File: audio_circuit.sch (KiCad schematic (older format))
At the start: 21 parts

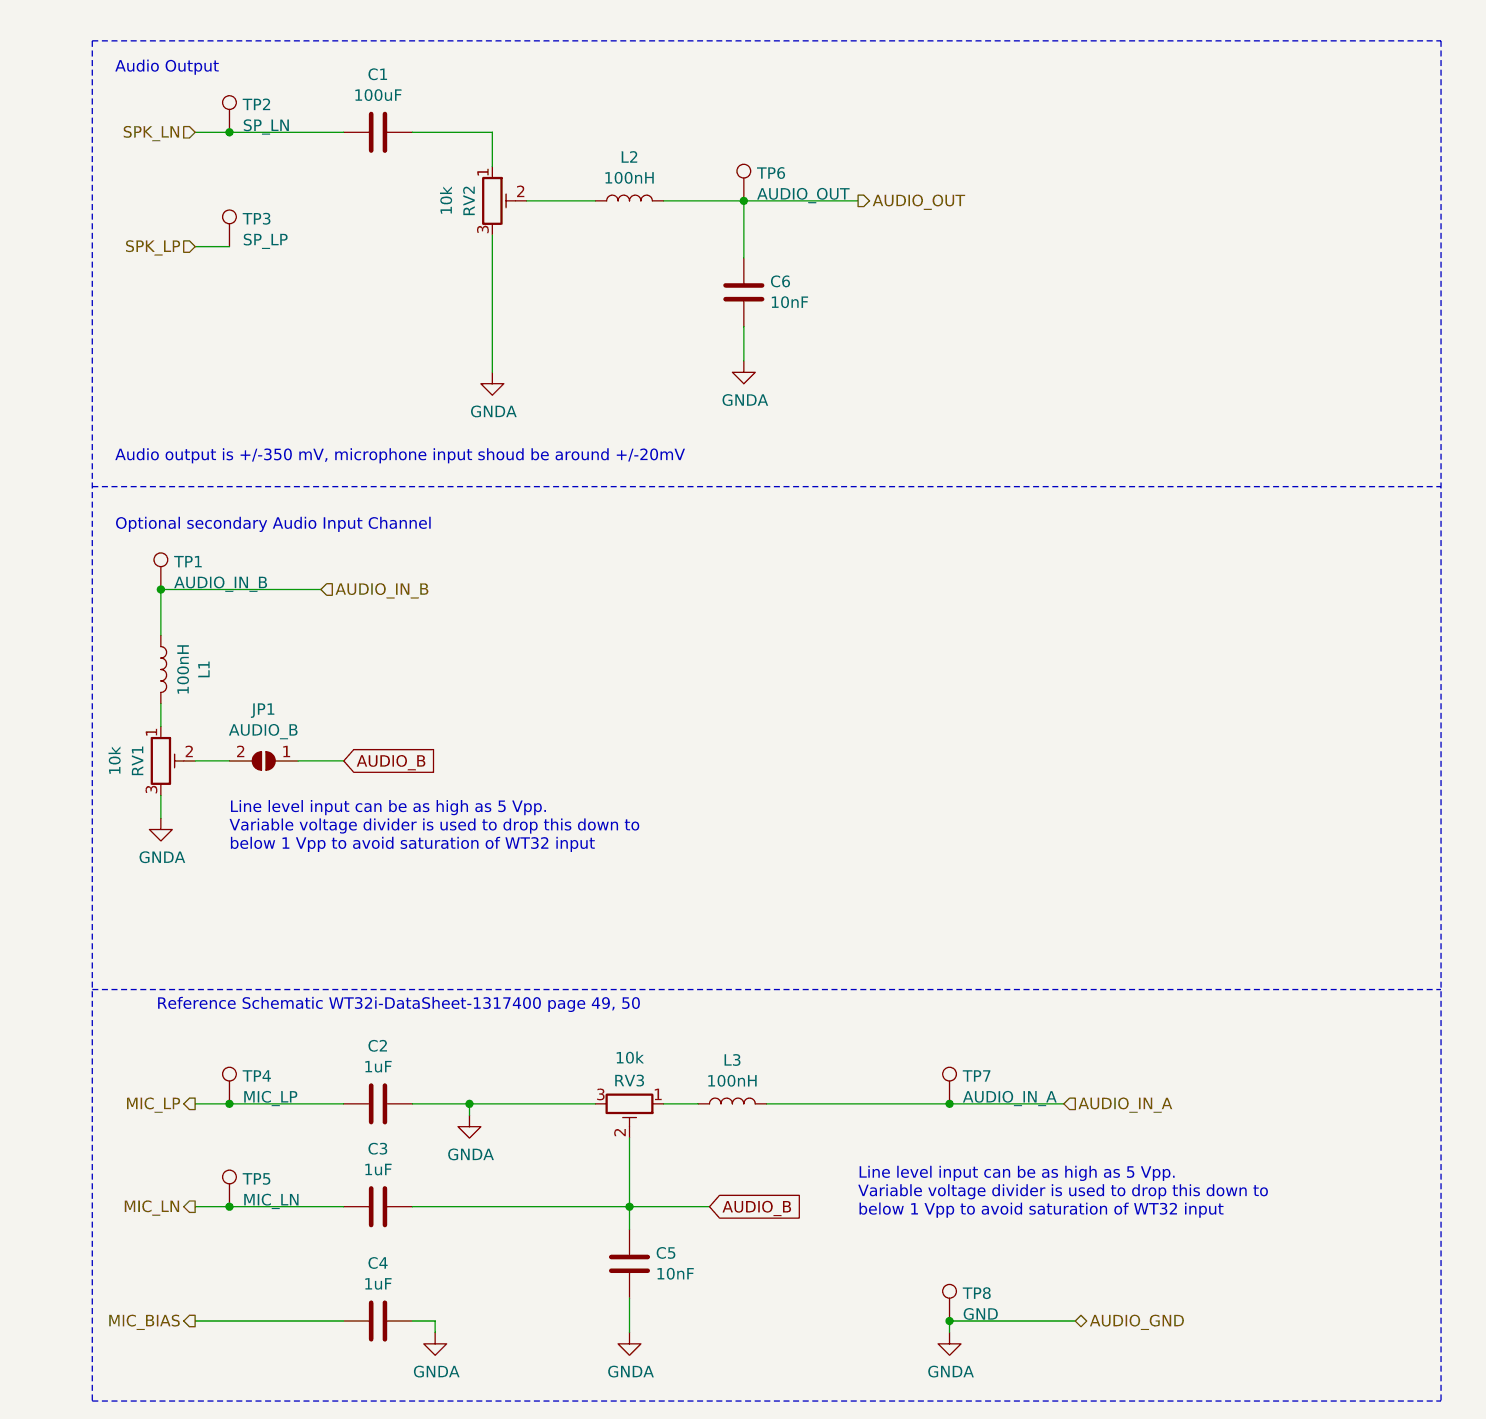
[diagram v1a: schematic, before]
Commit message: [#1] Refined Schematic
* Removed RTS CTS
* Added 15pF capacitator to audio IN+
* Removed PTT jumper
* Added pull-up jumper
* Added solder jmpr bypass to RV
* Changed button footprint to SMD version
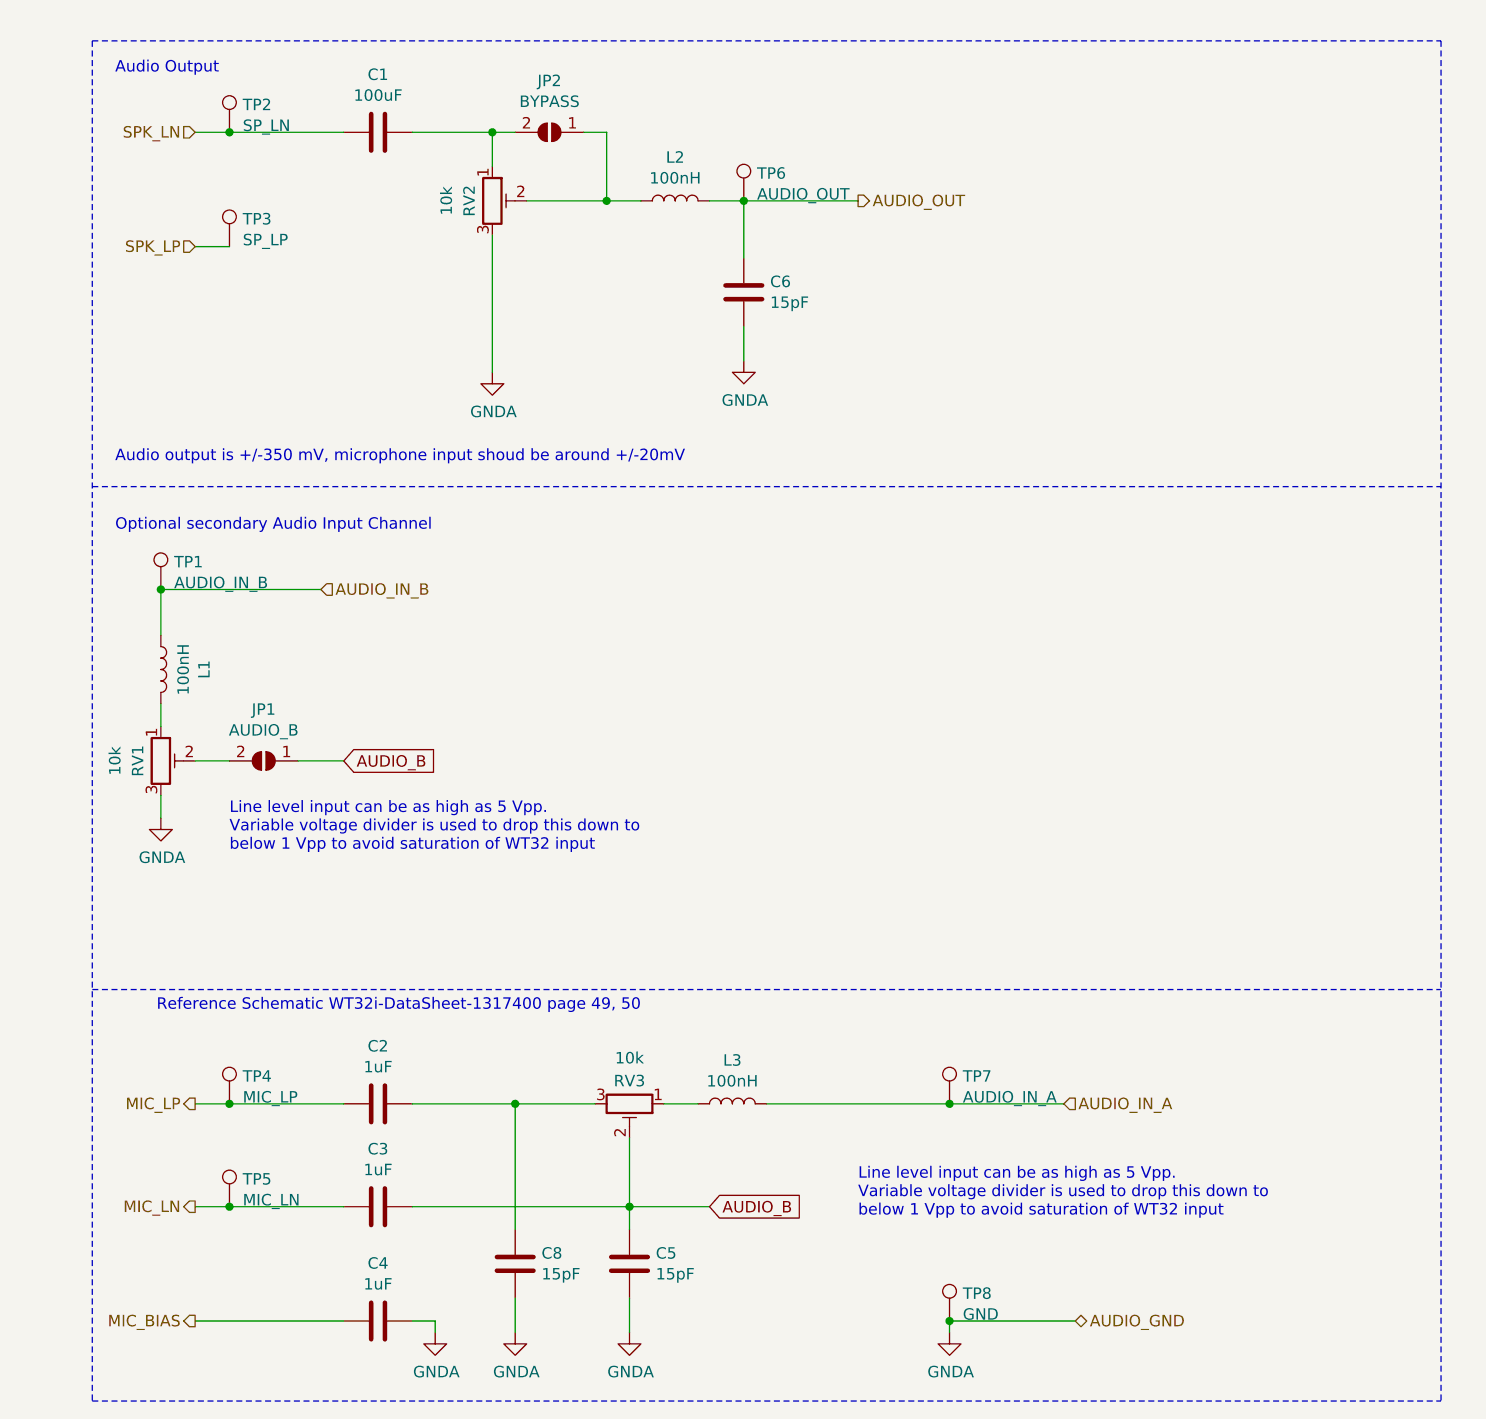
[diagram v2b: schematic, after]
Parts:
- added C8: 15pF, Capacitor_SMD:C_0805_2012Metric_Pad1.15x1.40mm_HandSolder, symbol Device:C
- added JP2: BYPASS, Jumper:SolderJumper-2_P1.3mm_Open_TrianglePad1.0x1.5mm, symbol Jumper:SolderJumper_2_Open
- C1: Mouser Best.Nr. 581-F980J107MSA -> TBD; Notes (none) -> Tantal neccessary?
- C2, C3, C4: Mouser Best.Nr. 581-F981V105MSA -> TBD; Notes (none) -> Tantal neccessary?
- C5, C6: value 10nF -> 15pF; Mouser Best.Nr. 710-885012207092 -> TBD; Notes (none) -> Tantal neccessary?
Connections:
- net GNDA: now also C8.2; no longer C2.1, RV3.3
- net at C1.1, RV2.1: now also JP2.2 (B)
- net at L2.1, RV2.2: now also JP2.1 (A)
- new net: C2.1, C8.1, RV3.3
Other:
- moved on the sheet: L2
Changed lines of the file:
@@
 EESchema Schematic File Version 4
 LIBS:bt-trx-dev-board-cache
-EELAYER 26 0
+EELAYER 29 0
 EELAYER END
 $Descr A4 11693 8268
@@
 F 2 "Capacitor_SMD:C_0805_2012Metric_Pad1.15x1.40mm_HandSolder" H 2088 6700 50  0001 C CNN
 F 3 "~" H 2050 6850 50  0001 C CNN
-F 4 "" H 300 0   50  0001 C CNN "Reichelt Best.Nr."
-F 5 "581-F981V105MSA" H 300 0   50  0001 C CNN "Mouser Best.Nr."
+F 4 "TBD" H 300 0   50  0001 C CNN "Mouser Best.Nr."
+F 5 "Tantal neccessary?" H 2050 6850 50  0001 C CNN "Notes"
 	1    2050 6850
 	0    1    1    0
@@
 F 2 "Inductor_SMD:L_0805_2012Metric_Pad1.15x1.40mm_HandSolder" H 3600 5900 50  0001 C CNN
 F 3 "~" H 3600 5900 50  0001 C CNN
-F 4 "" H 300 -100 50  0001 C CNN "Reichelt Best.Nr."
-F 5 "810-MLF2012DR10MT000" H 300 -100 50  0001 C CNN "Mouser Best.Nr."
+F 4 "810-MLF2012DR10MT000" H 300 -100 50  0001 C CNN "Mouser Best.Nr."
 	1    3600 5900
 	0    -1   -1   0
@@
 P 3150 6600
 F 0 "C5" H 3265 6646 50  0000 L CNN
-F 1 "10nF" H 3265 6555 50  0000 L CNN
+F 1 "15pF" H 3265 6555 50  0000 L CNN
 F 2 "Capacitor_SMD:C_0805_2012Metric_Pad1.15x1.40mm_HandSolder" H 3188 6450 50  0001 C CNN
 F 3 "~" H 3150 6600 50  0001 C CNN
-F 4 "" H 300 200 50  0001 C CNN "Reichelt Best.Nr."
-F 5 "710-885012207092" H 300 200 50  0001 C CNN "Mouser Best.Nr."
+F 4 "TBD" H 300 200 50  0001 C CNN "Mouser Best.Nr."
+F 5 "Tantal neccessary?" H 3150 6600 50  0001 C CNN "Notes"
 	1    3150 6600
 	1    0    0    -1
@@
 F 2 "Capacitor_SMD:C_0805_2012Metric_Pad1.15x1.40mm_HandSolder" H 2088 6200 50  0001 C CNN
 F 3 "~" H 2050 6350 50  0001 C CNN
-F 4 "" H 150 0   50  0001 C CNN "Reichelt Best.Nr."
-F 5 "581-F981V105MSA" H 150 0   50  0001 C CNN "Mouser Best.Nr."
+F 4 "TBD" H 150 0   50  0001 C CNN "Mouser Best.Nr."
+F 5 "Tantal neccessary?" H 2050 6350 50  0001 C CNN "Notes"
 	1    2050 6350
 	0    1    1    0
@@
 F 2 "Capacitor_SMD:C_0805_2012Metric_Pad1.15x1.40mm_HandSolder" H 2088 5750 50  0001 C CNN
 F 3 "~" H 2050 5900 50  0001 C CNN
-F 4 "" H 150 -100 50  0001 C CNN "Reichelt Best.Nr."
-F 5 "581-F981V105MSA" H 150 -100 50  0001 C CNN "Mouser Best.Nr."
+F 4 "TBD" H 150 -100 50  0001 C CNN "Mouser Best.Nr."
+F 5 "Tantal neccessary?" H 2050 5900 50  0001 C CNN "Notes"
 	1    2050 5900
 	0    1    1    0
 $EndComp
-Wire Wire Line
-	2450 5900 2450 5950
 $Comp
 L power:GNDA #PWR016
 U 1 1 5C1B2304
-P 2450 5950
-F 0 "#PWR016" H 2450 5700 50  0001 C CNN
-F 1 "GNDA" H 2455 5777 50  0000 C CNN
-F 2 "" H 2450 5950 50  0001 C CNN
-F 3 "" H 2450 5950 50  0001 C CNN
-	1    2450 5950
-	1    0    0    -1
-$EndComp
-Wire Wire Line
-	2450 5900 3000 5900
+P 2650 6900
+F 0 "#PWR016" H 2650 6650 50  0001 C CNN
+F 1 "GNDA" H 2655 6727 50  0000 C CNN
+F 2 "" H 2650 6900 50  0001 C CNN
+F 3 "" H 2650 6900 50  0001 C CNN
+	1    2650 6900
+	1    0    0    -1
+$EndComp
 Connection ~ 3150 6350
 Wire Wire Line
@@
 F 2 "Inductor_SMD:L_0805_2012Metric_Pad1.15x1.40mm_HandSolder" H 1100 4000 50  0001 C CNN
 F 3 "~" H 1100 4000 50  0001 C CNN
-F 4 "" H -2200 -2000 50  0001 C CNN "Reichelt Best.Nr."
-F 5 "810-MLF2012DR10MT000" H -2200 -2000 50  0001 C CNN "Mouser Best.Nr."
+F 4 "810-MLF2012DR10MT000" H -2200 -2000 50  0001 C CNN "Mouser Best.Nr."
 	1    1100 4000
 	1    0    0    -1
@@
 F 2 "Capacitor_SMD:C_0805_2012Metric_Pad1.15x1.40mm_HandSolder" H 2088 1500 50  0001 C CNN
 F 3 "~" H 2050 1650 50  0001 C CNN
-F 4 "" H 150 -4350 50  0001 C CNN "Reichelt Best.Nr."
-F 5 "581-F980J107MSA" H 150 -4350 50  0001 C CNN "Mouser Best.Nr."
+F 4 "TBD" H 150 -4350 50  0001 C CNN "Mouser Best.Nr."
+F 5 "Tantal neccessary?" H 2050 1650 50  0001 C CNN "Notes"
 	1    2050 1650
 	0    1    1    0
@@
 Wire Wire Line
 	3150 6050 3150 6350
-Wire Wire Line
-	2200 5900 2450 5900
-Connection ~ 2450 5900
-Wire Wire Line
-	2200 6350 3150 6350
 $Comp
 L Connector:TestPoint TP7
@@
 L Device:L L2
 U 1 1 5CD0D38F
-P 3150 1950
-F 0 "L2" V 3340 1950 50  0000 C CNN
-F 1 "100nH" V 3249 1950 50  0000 C CNN
-F 2 "Inductor_SMD:L_0805_2012Metric_Pad1.15x1.40mm_HandSolder" H 3150 1950 50  0001 C CNN
-F 3 "~" H 3150 1950 50  0001 C CNN
-F 4 "" H -150 -4050 50  0001 C CNN "Reichelt Best.Nr."
-F 5 "810-MLF2012DR10MT000" H -150 -4050 50  0001 C CNN "Mouser Best.Nr."
-	1    3150 1950
+P 3350 1950
+F 0 "L2" V 3540 1950 50  0000 C CNN
+F 1 "100nH" V 3449 1950 50  0000 C CNN
+F 2 "Inductor_SMD:L_0805_2012Metric_Pad1.15x1.40mm_HandSolder" H 3350 1950 50  0001 C CNN
+F 3 "~" H 3350 1950 50  0001 C CNN
+F 4 "810-MLF2012DR10MT000" H 50  -4050 50  0001 C CNN "Mouser Best.Nr."
+	1    3350 1950
 	0    -1   -1   0
 $EndComp
@@
 P 3650 2350
 F 0 "C6" H 3765 2396 50  0000 L CNN
-F 1 "10nF" H 3765 2305 50  0000 L CNN
+F 1 "15pF" H 3765 2305 50  0000 L CNN
 F 2 "Capacitor_SMD:C_0805_2012Metric_Pad1.15x1.40mm_HandSolder" H 3688 2200 50  0001 C CNN
 F 3 "~" H 3650 2350 50  0001 C CNN
-F 4 "" H 800 -4050 50  0001 C CNN "Reichelt Best.Nr."
-F 5 "710-885012207092" H 800 -4050 50  0001 C CNN "Mouser Best.Nr."
+F 4 "TBD" H 800 -4050 50  0001 C CNN "Mouser Best.Nr."
+F 5 "Tantal neccessary?" H 3650 2350 50  0001 C CNN "Notes"
 	1    3650 2350
 	1    0    0    -1
@@
 Wire Wire Line
 	3650 1950 4150 1950
-Wire Wire Line
-	3300 1950 3650 1950
-Wire Wire Line
-	2700 1950 3000 1950
+$Comp
+L Jumper:SolderJumper_2_Open JP2
+U 1 1 5D4B6C36
+P 2800 1650
+F 0 "JP2" H 2800 1425 50  0000 C CNN
+F 1 "BYPASS" H 2800 1516 50  0000 C CNN
+F 2 "Jumper:SolderJumper-2_P1.3mm_Open_TrianglePad1.0x1.5mm" H 2800 1650 50  0001 C CNN
+F 3 "~" H 2800 1650 50  0001 C CNN
+F 4 "-" H 1250 -2750 50  0001 C CNN "Mouser Best.Nr."
+	1    2800 1650
+	-1   0    0    1
+$EndComp
+Wire Wire Line
+	2650 1650 2550 1650
+Connection ~ 2550 1650
+Wire Wire Line
+	3050 1650 3050 1950
+Wire Wire Line
+	3050 1950 3200 1950
+Wire Wire Line
+	3500 1950 3650 1950
+Wire Wire Line
+	2950 1650 3050 1650
+Wire Wire Line
+	2700 1950 3050 1950
+Connection ~ 3050 1950
+$Comp
+L Device:C C8
+U 1 1 5D4A378C
+P 2650 6600
+F 0 "C8" H 2765 6646 50  0000 L CNN
+F 1 "15pF" H 2765 6555 50  0000 L CNN
+F 2 "Capacitor_SMD:C_0805_2012Metric_Pad1.15x1.40mm_HandSolder" H 2688 6450 50  0001 C CNN
+F 3 "~" H 2650 6600 50  0001 C CNN
+F 4 "TBD" H -200 200 50  0001 C CNN "Mouser Best.Nr."
+F 5 "Tantal neccessary?" H 2650 6600 50  0001 C CNN "Notes"
+	1    2650 6600
+	1    0    0    -1
+$EndComp
+Wire Wire Line
+	2650 6750 2650 6900
+Wire Wire Line
+	2200 5900 2650 5900
+Wire Wire Line
+	2200 6350 3150 6350
+Wire Wire Line
+	2650 6450 2650 5900
+Connection ~ 2650 5900
+Wire Wire Line
+	2650 5900 3000 5900
 $EndSCHEMATC
